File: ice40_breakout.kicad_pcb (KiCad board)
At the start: 4 copper layers, 80 x 100 mm, 248 parts, among them J1 Conn_01x10, J2 Conn_01x08, J3 Conn_01x06, J4 Conn_01x08, J5 USB_B_Micro, J6 7-17 V IN, Q1 DMP3099L-7, Q2 Q_NMOS_GSD, Q3 Q_NMOS_GSD, Q4 Q_NMOS_GSD, SW1 SW_Push, SW2 SW_Push, SW3 SW_Push, SW4 SW_Push, SW5 SW_Push, SW6 SW_Push, SW7 JS202011SCQN, SW8 JS202011SCQN, SW9 JS202011SCQN, U1 ICE40HX4K-TQ144, U10 MAX40200AUK, U11 SN74LVC2G07DCKR, U12 TPS562201, U13 SN74AXC4T245PWR, U14 MIC5365-3.3YC5, U15 MAX40200AUK, U16 SN74LVC2T45DCUR, U17 SN74LVC2T45DCUR, U18 SN74LVC2T45DCUR, U19 SN74LVC2T45DCUR, U2 IS61WV5128EDBLL-10TLI, U20 MAX11614, U21 MAX40200AUK, U22 MAX40200AUK, U23 MAX40200AUK, U3 93LCxxBT-I_OT, U4 FT2232H, U5 IS25LP080D, U6 TLV62568APDRLR, U7 TLV62568APDRLR, U8 TXS0108EPW, U9 TXS0108EPW, Y1 ECS-3225S33-120-FN-TR, Y2 ECS-3225S33-500-FN-TR

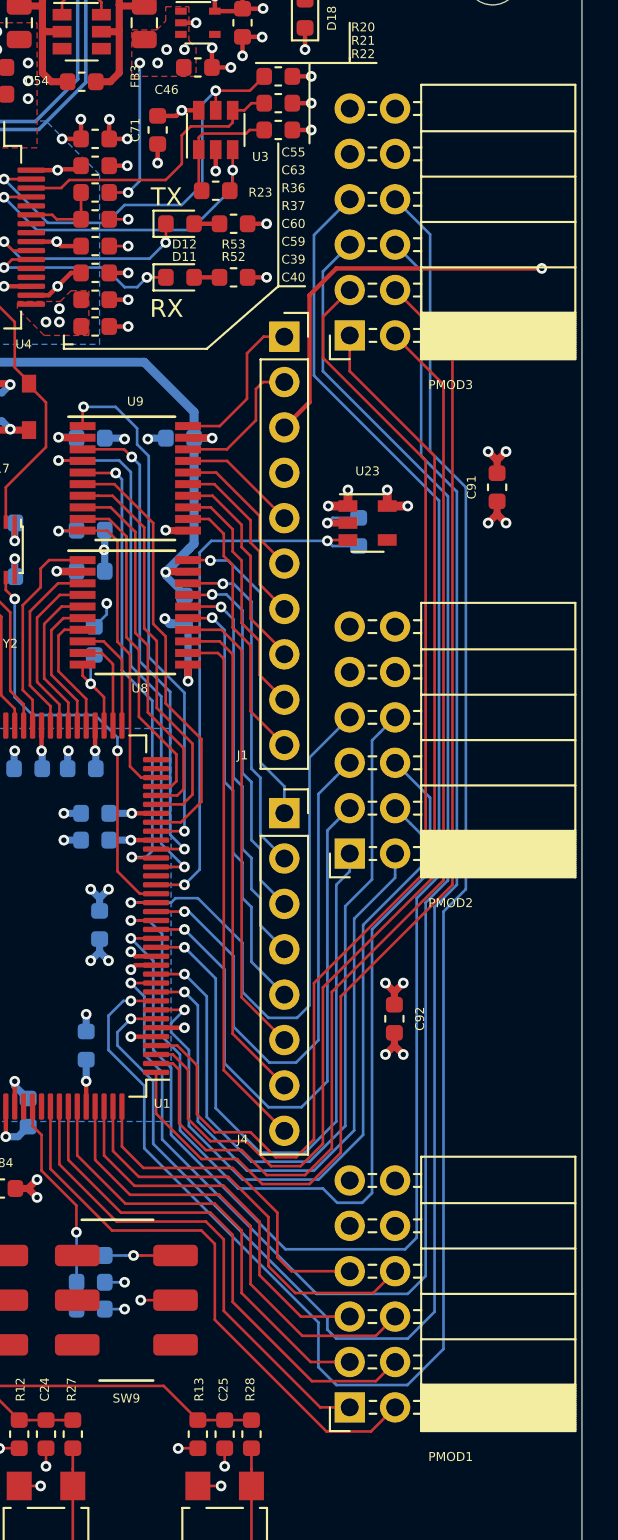
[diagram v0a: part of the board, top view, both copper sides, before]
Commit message: Fixed rotated PMODs
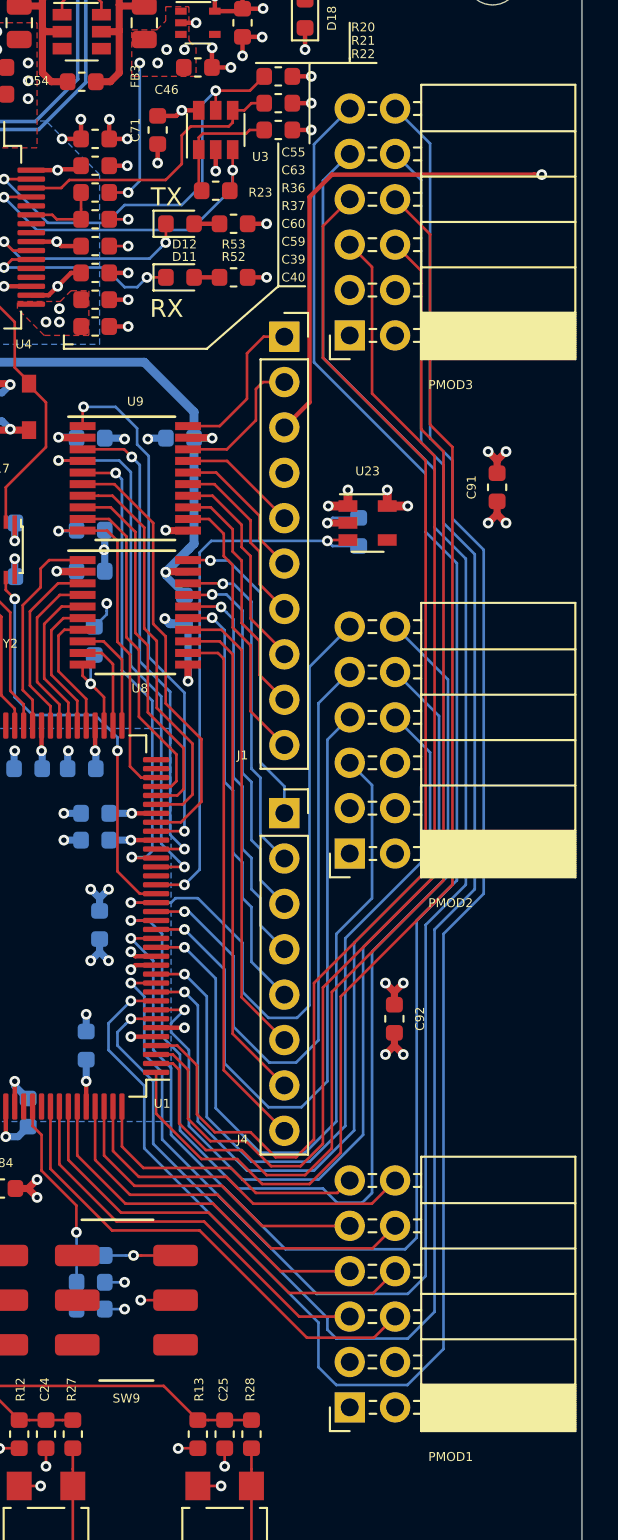
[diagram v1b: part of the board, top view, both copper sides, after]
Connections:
- PMOD1 pad 1: P7_1 -> /Header/PMOD_3V3
- PMOD1 pad 10: GND -> P2_1
- PMOD1 pad 11: /Header/PMOD_3V3 -> P7_1
- PMOD1 pad 12: /Header/PMOD_3V3 -> P1_1
- PMOD1 pad 2: P1_1 -> /Header/PMOD_3V3
- PMOD1 pad 3: P8_1 -> GND
- PMOD1 pad 4: P2_1 -> GND
- PMOD1 pad 5: P9_1 -> P10_1
- PMOD1 pad 6: P3_1 -> P4_1
- PMOD1 pad 7: P10_1 -> P9_1
- PMOD1 pad 8: P4_1 -> P3_1
- PMOD1 pad 9: GND -> P8_1
- PMOD2 pad 1: /Header/P7_2 -> /Header/PMOD_3V3
- PMOD2 pad 10: GND -> /Header/P8_2
- PMOD2 pad 11: /Header/PMOD_3V3 -> /Header/P1_2
- PMOD2 pad 12: /Header/PMOD_3V3 -> /Header/P7_2
- PMOD2 pad 2: /Header/P1_2 -> /Header/PMOD_3V3
- PMOD2 pad 3: /Header/P8_2 -> GND
- PMOD2 pad 4: /Header/P2_2 -> GND
- PMOD2 pad 5: /Header/P9_2 -> /Header/P4_2
- PMOD2 pad 6: /Header/P3_2 -> /Header/P10_2
- PMOD2 pad 7: /Header/P10_2 -> /Header/P3_2
- PMOD2 pad 8: /Header/P4_2 -> /Header/P9_2
- PMOD2 pad 9: GND -> /Header/P2_2
- PMOD3 pad 1: /Header/P7_3 -> /Header/PMOD_3V3
- PMOD3 pad 10: GND -> /Header/P8_3
- PMOD3 pad 11: /Header/PMOD_3V3 -> /Header/P1_3
- PMOD3 pad 12: /Header/PMOD_3V3 -> /Header/P7_3
- PMOD3 pad 2: /Header/P1_3 -> /Header/PMOD_3V3
- PMOD3 pad 3: /Header/P8_3 -> GND
- PMOD3 pad 4: /Header/P2_3 -> GND
- PMOD3 pad 5: /Header/P9_3 -> /Header/P4_3
- PMOD3 pad 6: /Header/P3_3 -> /Header/P10_3
- PMOD3 pad 7: /Header/P10_3 -> /Header/P3_3
- PMOD3 pad 8: /Header/P4_3 -> /Header/P9_3
- PMOD3 pad 9: GND -> /Header/P2_3
- U1 pad 1: /Header/P2_3 -> /Header/P9_3
- U1 pad 10: /Header/P1_2 -> /Header/P9_2
- U1 pad 11: /Header/P9_3 -> /Header/P2_3
- U1 pad 12: /Header/P4_2 -> /Header/P10_2
- U1 pad 136: P1_1 -> P4_1
- U1 pad 137: P7_1 -> P10_1
- U1 pad 138: P2_1 -> P3_1
- U1 pad 139: P8_1 -> P9_1
- U1 pad 141: P3_1 -> P2_1
- U1 pad 142: P9_1 -> P8_1
- U1 pad 143: P4_1 -> P1_1
- U1 pad 144: P10_1 -> P7_1
- U1 pad 15: /Header/P7_2 -> /Header/P4_2
- U1 pad 16: /Header/P10_3 -> /Header/P1_3
- U1 pad 17: /Header/P8_2 -> /Header/P3_2
- U1 pad 18: /Header/P3_2 -> /Header/P7_2
- U1 pad 19: /Header/P9_2 -> /Header/P2_2
- U1 pad 2: /Header/P1_3 -> /Header/P10_3
- U1 pad 20: /Header/P10_2 -> /Header/P1_2
- U1 pad 3: /Header/P7_3 -> /Header/P4_3
- U1 pad 4: /Header/P8_3 -> /Header/P3_3
- U1 pad 7: /Header/P3_3 -> /Header/P8_3
- U1 pad 8: /Header/P2_2 -> /Header/P8_2
- U1 pad 9: /Header/P4_3 -> /Header/P7_3
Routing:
- net /Header/P7_3: track 63.9 -> 108.0 mm, vias 0 -> 1
- net /Header/P1_3: track 64.1 -> 98.3 mm, vias 0 -> 1
- net /Header/P4_3: track 102.3 -> 68.9 mm, vias 1 -> 0
- net /Header/P8_3: track 66.6 -> 98.4 mm, vias 0 -> 1
- net /Header/P2_3: track 67.2 -> 97.3 mm, vias 0 -> 1
- net /Header/P7_2: track 35.1 -> 62.2 mm
- net /Header/P10_3: track 92.4 -> 69.1 mm, vias 1 -> 0
- net /Header/P3_3: track 92.5 -> 71.7 mm, vias 1 -> 0
- net /Header/P9_3: track 91.4 -> 72.3 mm, vias 1 -> 0
- net /Header/P8_2: track 33.2 -> 49.5 mm
- net /Header/P3_2: track 53.8 -> 38.3 mm
- net /Header/P9_2: track 31.7 -> 45.7 mm
- net P1_1: track 31.9 -> 20.0 mm
- net P7_1: track 27.5 -> 16.4 mm
- net /Header/P10_2: track 33.2 -> 40.5 mm
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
